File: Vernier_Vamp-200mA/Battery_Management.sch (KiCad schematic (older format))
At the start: 48 parts, among them J4 Conn_02x07_Odd_Even, Q1 Si4447ADY, Q2 IRF8707PbF, SW1 DPDT_Hirose, U1 LM4040DBZ-5, U2 LM4040DBZ-5, U3 LM393

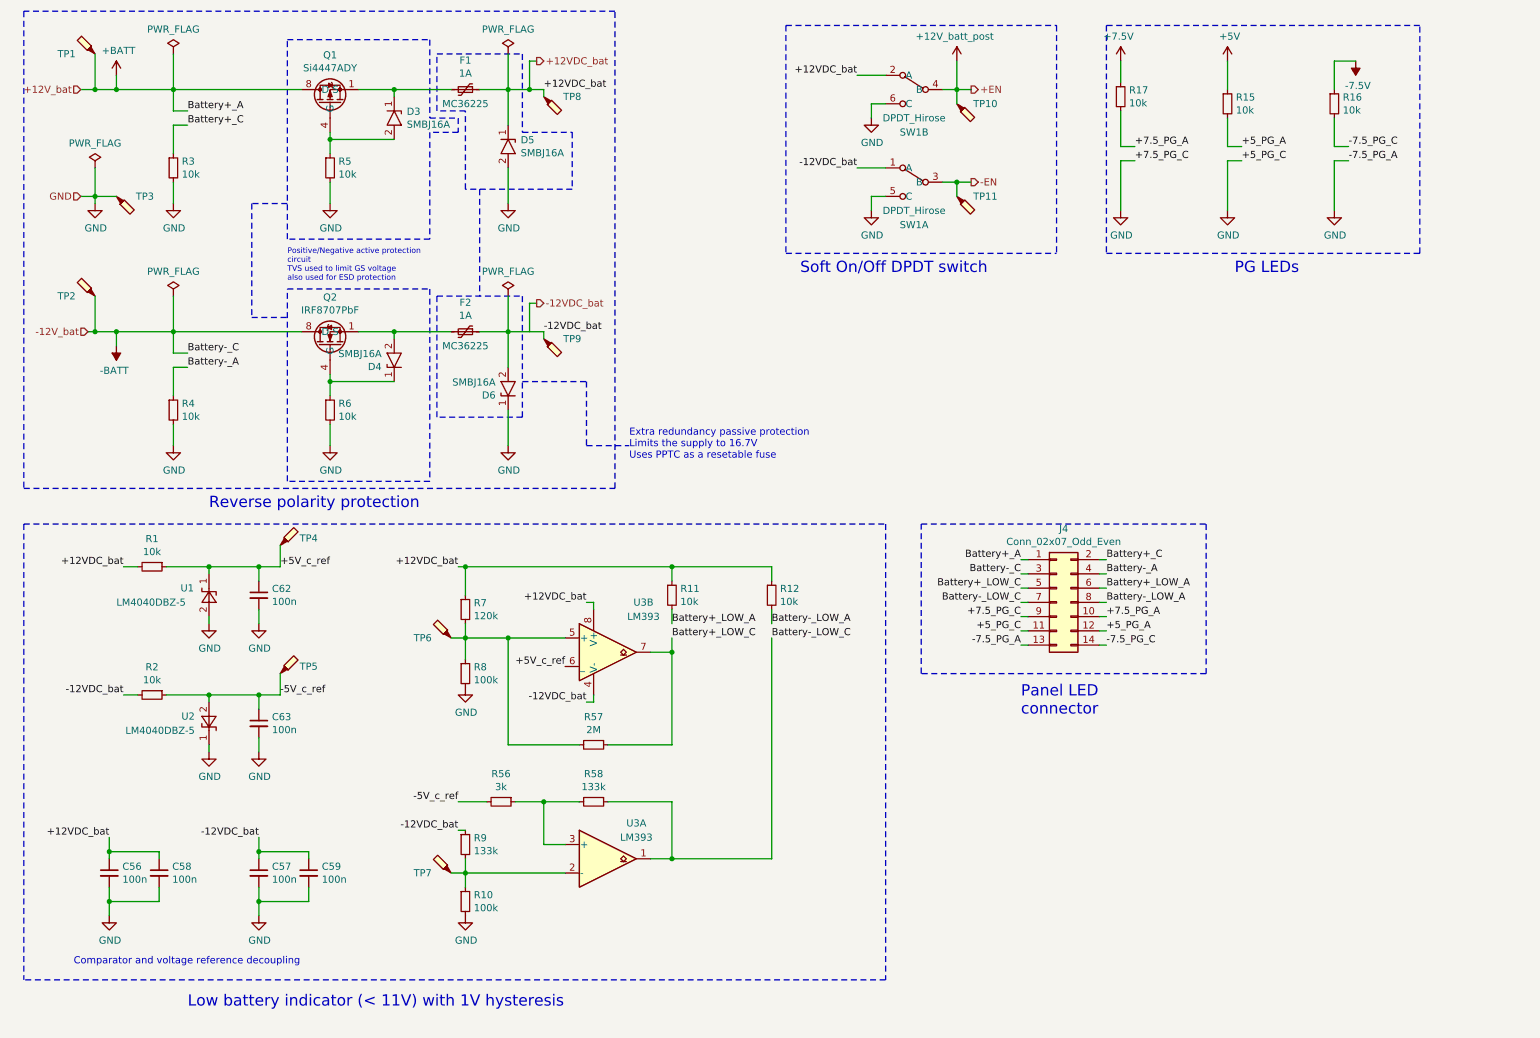
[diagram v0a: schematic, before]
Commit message: Schematic and layout changes
Schematic updates:
- Added extra comments
- Added description (BNC channels)
- Moved mounting holes to the title block
- Added an option for connecting low battery indicatior LEDs to either +12V or GND (Comparator pulls to -12V)
- Added a 0R resistor for connecting +12V to Vin of nano
Layout:
- Added board ID and datecode on both sides
- Fixed priority of GND copper islands that were causing issues
- Changed the ground plane to be solid on the connection point (still not ideal but better)
- All components with thermal vias require tented vias so left as default
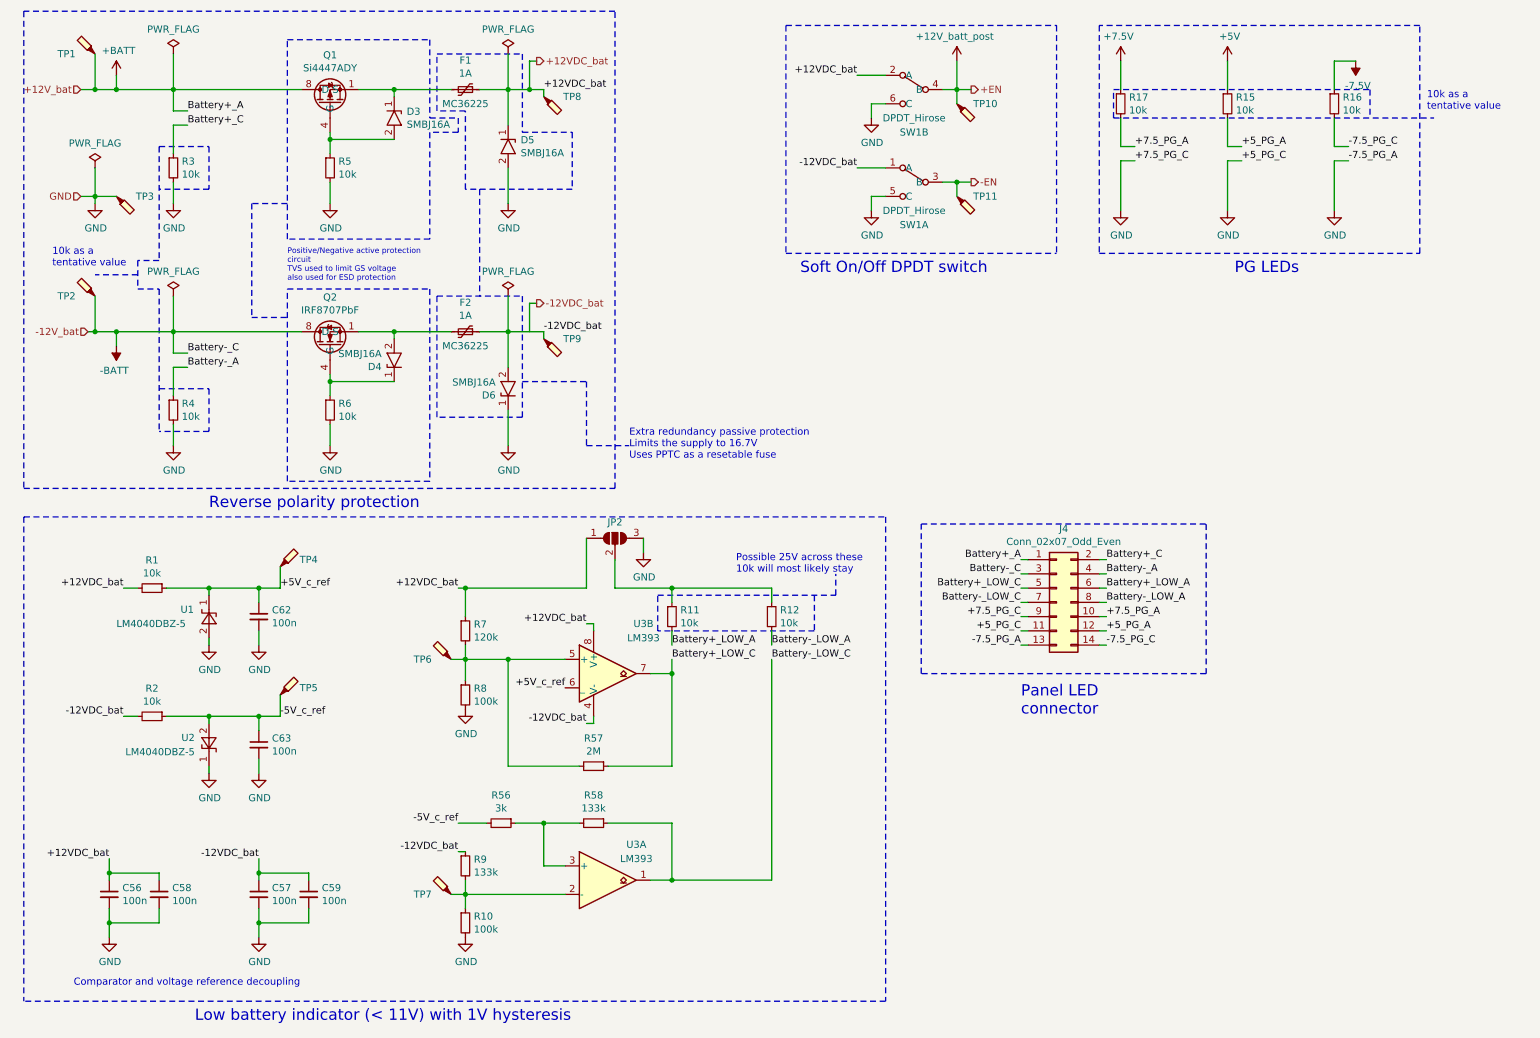
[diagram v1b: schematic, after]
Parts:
- added JP2: SolderJumper_3_Open, Jumper:SolderJumper-3_P1.3mm_Open_Pad1.0x1.5mm_NumberLabels, symbol Jumper:SolderJumper_3_Open
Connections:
- net +12VDC_bat: now also JP2.1 (A); no longer R11.1, R12.1
- net GND: now also JP2.3 (B)
- new net: JP2.2 (C), R11.1, R12.1
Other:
- note added: "10k as a\ntentative value"
- note added: "Possible 25V across these\n10k will most likely stay"
- moved on the sheet: C56, C57, C58, C59, C62, C63, R1, R10, R11, R12, R17, R2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

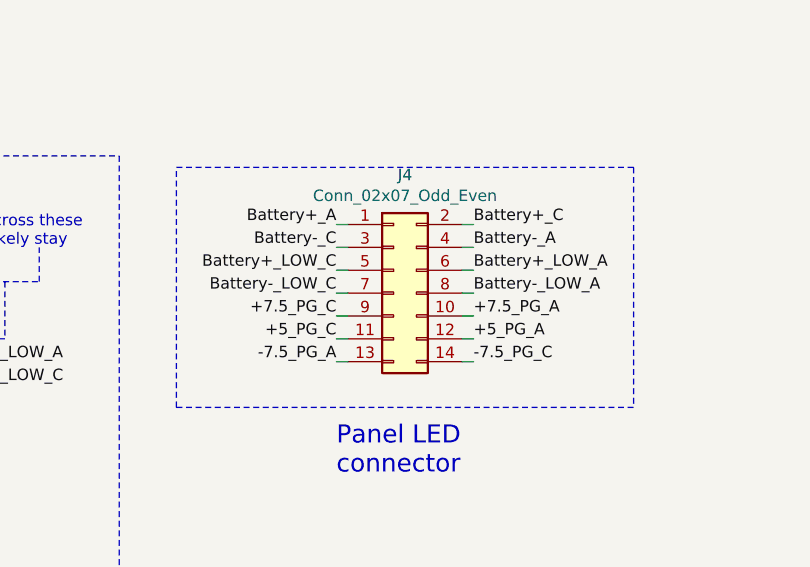
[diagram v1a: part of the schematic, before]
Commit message: 1.0D Update
LCCD changes
-Addition of trigger for calibration
-PCB optimisation

HCCD changes
-New output stage designed
-Changes from 1.0C applied to HCCD
-New more optimised layout
-New shielding over analog section
-Addition of trigger for calibration

New symbols and footprint creation
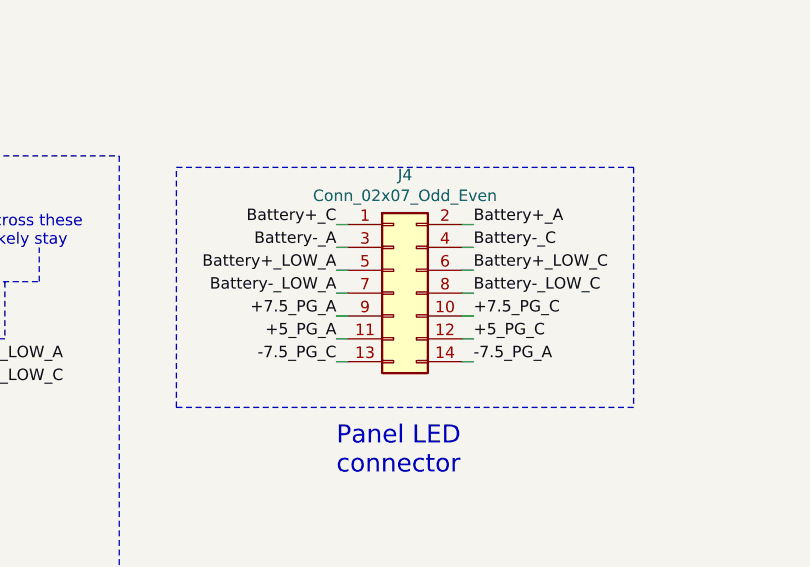
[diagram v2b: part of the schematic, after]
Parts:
- J4: footprint Connector_Hirose:Hirose_DF11-14DP-2DSA_2x07_P2.00mm_Vertical -> Connector_IDC:IDC-Header_2x07_P2.54mm_Vertical
- SW1: footprint Connector_Hirose:Hirose_DF11-6DP-2DSA_2x03_P2.00mm_Vertical -> Connector_IDC:IDC-Header_2x03_P2.54mm_Vertical
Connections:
- net +5_PG_A: now also J4.11 (Pin_11); no longer J4.12 (Pin_12)
- net +7.5_PG_A: now also J4.9 (Pin_9); no longer J4.10 (Pin_10)
- net +BATT: now also J4.2 (Pin_2); no longer J4.1 (Pin_1)
- net -7.5_PG_C: now also J4.13 (Pin_13); no longer J4.14 (Pin_14)
- net -BATT: now also J4.4 (Pin_4); no longer J4.3 (Pin_3)
- net Battery+_C: now also J4.1 (Pin_1); no longer J4.2 (Pin_2)
- net Battery+_LOW_A: now also J4.5 (Pin_5); no longer J4.6 (Pin_6)
- net Battery+_LOW_C: now also J4.6 (Pin_6); no longer J4.5 (Pin_5)
- net Battery-_A: now also J4.3 (Pin_3); no longer J4.4 (Pin_4)
- net Battery-_LOW_A: now also J4.7 (Pin_7); no longer J4.8 (Pin_8)
- net Battery-_LOW_C: now also J4.8 (Pin_8); no longer J4.7 (Pin_7)
- net GND: now also J4.10 (Pin_10), J4.12 (Pin_12), J4.14 (Pin_14); no longer J4.11 (Pin_11), J4.13 (Pin_13), J4.9 (Pin_9)
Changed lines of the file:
@@
 encoding utf-8
 Sheet 3 7
-Title "\"Vernier Vamp\" Coil Driver - 200mA"
+Title "\"Vernier Vamp\" Coil Driver - HCCD"
 Date "2020-04-27"
-Rev "1.0B"
+Rev "1.0D"
 Comp "Strathclyde University"
 Comment1 "Designed by: Marcin Mrozowski"
@@
 F 0 "SW1" H 7050 500 50  0000 C CNN
 F 1 "DPDT_Hirose" H 7050 600 50  0000 C CNN
-F 2 "Connector_Hirose:Hirose_DF11-6DP-2DSA_2x03_P2.00mm_Vertical" H 7050 1000 50  0001 C CNN
+F 2 "Connector_IDC:IDC-Header_2x03_P2.54mm_Vertical" H 7050 1000 50  0001 C CNN
 F 3 "" H 7050 1000 50  0001 C CNN
 	2    7050 1000
@@
 Wire Wire Line
 	7850 4500 7800 4500
-Text Label 7800 5100 2    50   ~ 0
+Text Label 8400 5100 0    50   ~ 0
 -7.5_PG_A
-Text Label 8400 5000 0    50   ~ 0
+Text Label 7800 5000 2    50   ~ 0
 +5_PG_A
-Text Label 8400 4900 0    50   ~ 0
+Text Label 7800 4900 2    50   ~ 0
 +7.5_PG_A
-Text Label 8400 4800 0    50   ~ 0
+Text Label 7800 4800 2    50   ~ 0
 Battery-_LOW_A
-Text Label 8400 4700 0    50   ~ 0
+Text Label 7800 4700 2    50   ~ 0
 Battery+_LOW_A
-Text Label 8400 4600 0    50   ~ 0
+Text Label 7800 4600 2    50   ~ 0
 Battery-_A
-Text Label 8400 4500 0    50   ~ 0
+Text Label 7800 4500 2    50   ~ 0
 Battery+_C
 Wire Notes Line
@@
 F 0 "J4" H 8100 5317 50  0000 C CNN
 F 1 "Conn_02x07_Odd_Even" H 8100 5226 50  0000 C CNN
-F 2 "Connector_Hirose:Hirose_DF11-14DP-2DSA_2x07_P2.00mm_Vertical" H 8050 4800 50  0001 C CNN
+F 2 "Connector_IDC:IDC-Header_2x07_P2.54mm_Vertical" H 8050 4800 50  0001 C CNN
 F 3 "~" H 8050 4800 50  0001 C CNN
 	1    8050 4800
 	1    0    0    -1
 $EndComp
-Text Label 8400 5100 0    50   ~ 0
+Text Label 7800 5100 2    50   ~ 0
 -7.5_PG_C
-Text Label 7800 5000 2    50   ~ 0
+Text Label 8400 5000 0    50   ~ 0
 +5_PG_C
-Text Label 7800 4900 2    50   ~ 0
+Text Label 8400 4900 0    50   ~ 0
 +7.5_PG_C
-Text Label 7800 4800 2    50   ~ 0
+Text Label 8400 4800 0    50   ~ 0
 Battery-_LOW_C
-Text Label 7800 4700 2    50   ~ 0
+Text Label 8400 4700 0    50   ~ 0
 Battery+_LOW_C
-Text Label 7800 4600 2    50   ~ 0
+Text Label 8400 4600 0    50   ~ 0
 Battery-_C
-Text Label 7800 4500 2    50   ~ 0
+Text Label 8400 4500 0    50   ~ 0
 Battery+_A
 Text HLabel 7450 1200 2    50   Output ~ 0
@@
 F 0 "SW1" H 7050 1150 50  0000 C CNN
 F 1 "DPDT_Hirose" H 7050 1250 50  0000 C CNN
-F 2 "Connector_Hirose:Hirose_DF11-6DP-2DSA_2x03_P2.00mm_Vertical" H 7050 1650 50  0001 C CNN
+F 2 "Connector_IDC:IDC-Header_2x03_P2.54mm_Vertical" H 7050 1650 50  0001 C CNN
 F 3 "" H 7050 1650 50  0001 C CNN
 	1    7050 1650
